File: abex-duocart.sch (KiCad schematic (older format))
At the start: 12 parts, among them P1 0877159106, P2 CONN_01X01, P3 CONN_01X01, P4 CONN_01X01, P5 CONN_01X01, SW2 SW_Push

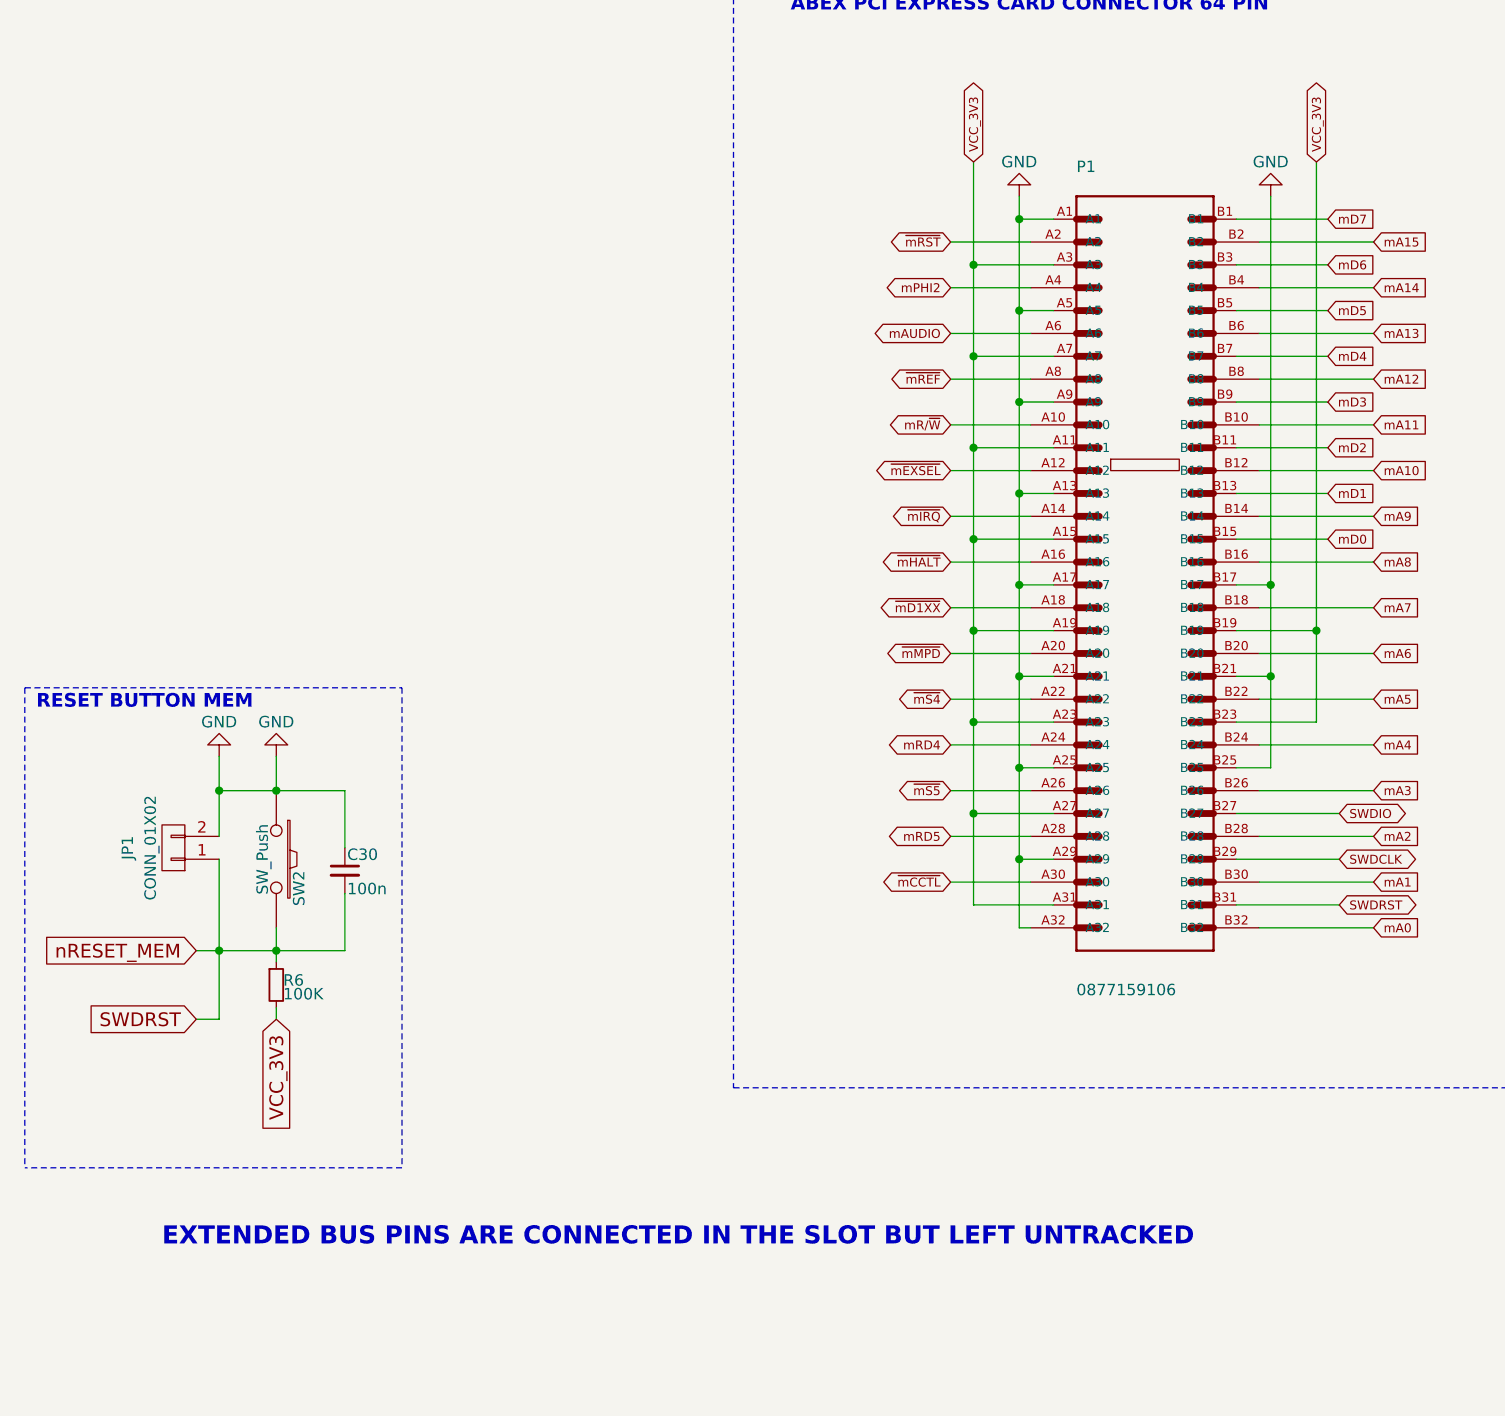
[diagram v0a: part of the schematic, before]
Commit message: Added the CardDetect. Added the A31 +5V pin
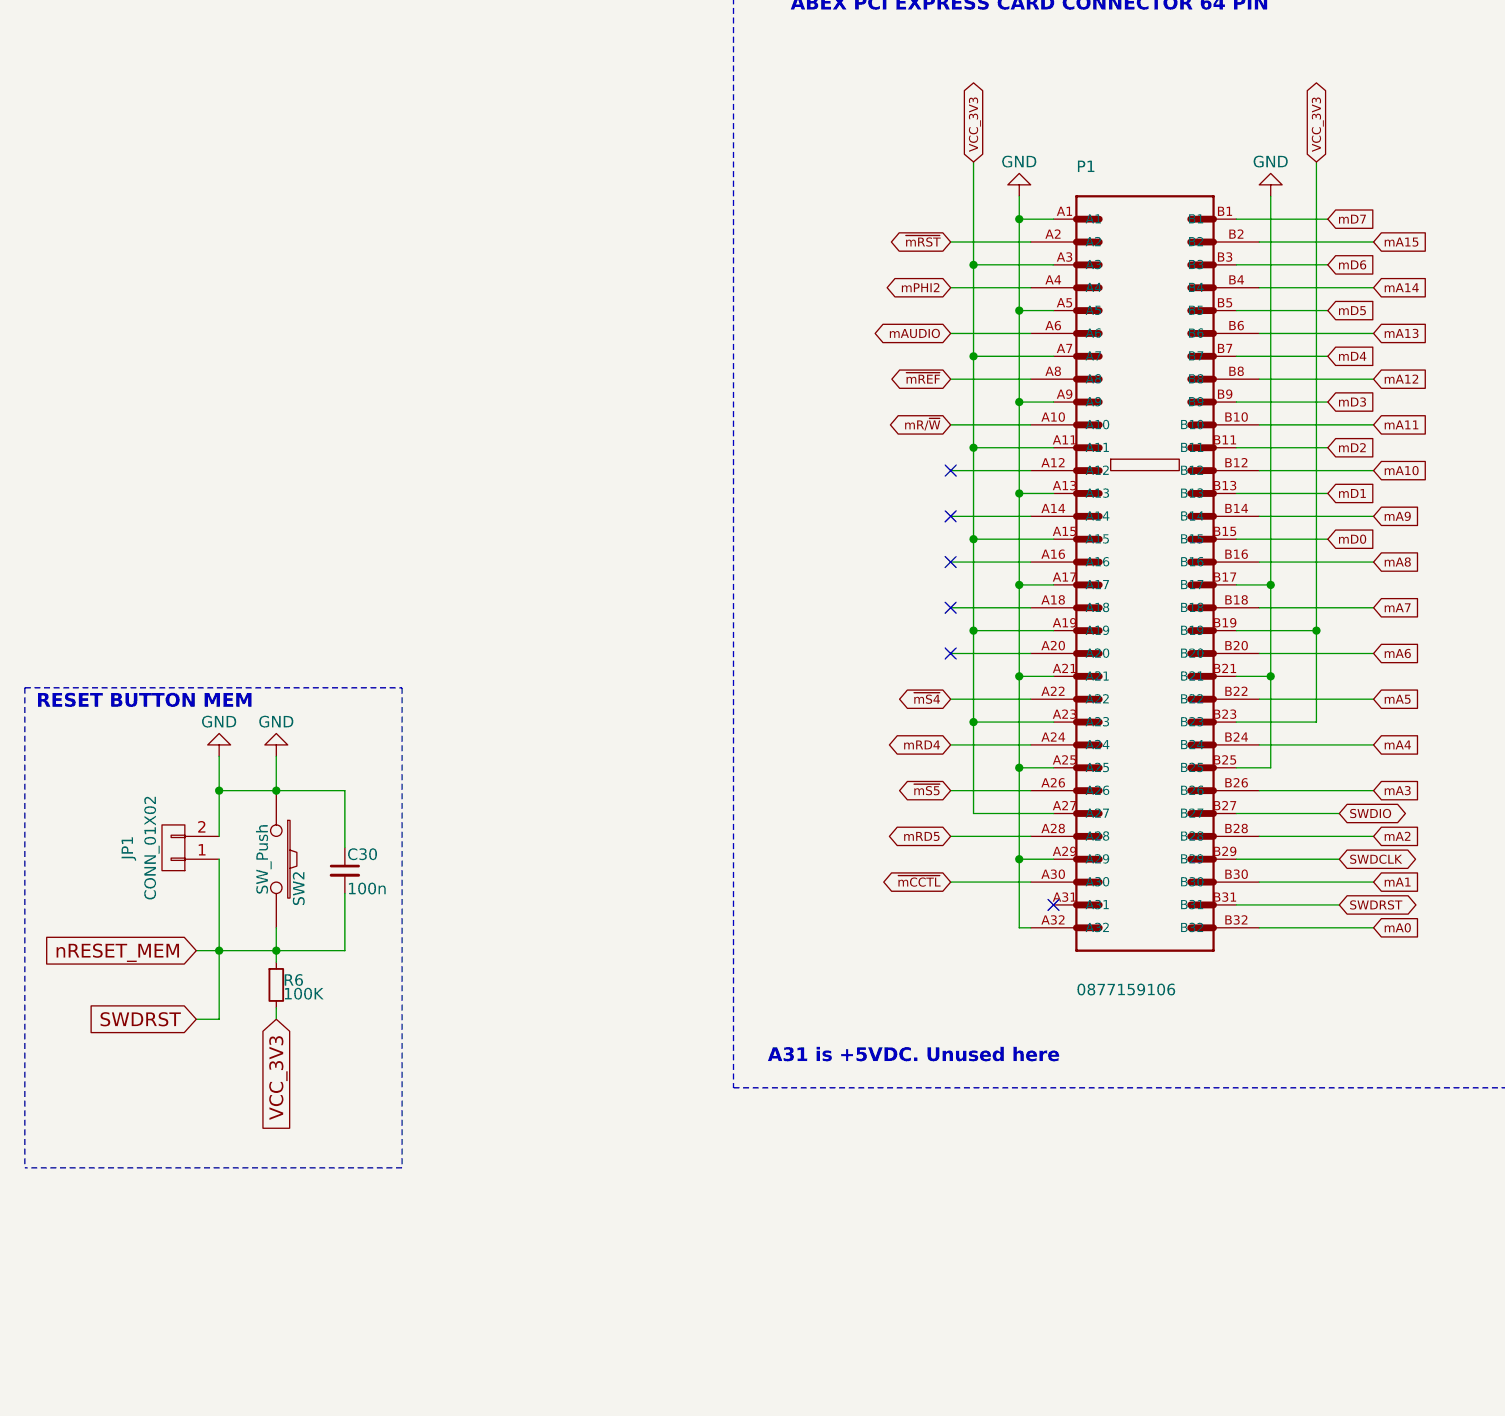
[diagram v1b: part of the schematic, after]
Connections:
- net VCC: no longer P1.A31
- net ~mD1XX: no longer names the net of P1.A18
- net ~mEXSEL: no longer names the net of P1.A12
- net ~mHALT: no longer names the net of P1.A16
- net ~mIRQ: no longer names the net of P1.A14
- net ~mMPD: no longer names the net of P1.A20
- no-connect marks 8 -> 14
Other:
- note added: "A31 is +5VDC. Unused here"
- note removed: "EXTENDED BUS PINS ARE CONNECTED IN THE SLOT BUT LEFT UNTRACKED"
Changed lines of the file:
@@
 LIBS:Graphic
 LIBS:GPU
-LIBS:ft232rl
 LIBS:FPGA_Xilinx_Virtex7
 LIBS:FPGA_Xilinx_Virtex6
@@
 Text GLabel 4750 2850 0    39   BiDi ~ 0
 mAUDIO
-Text GLabel 4750 3050 0    39   BiDi ~ 0
-~mREF
 Text GLabel 4850 2100 1    39   BiDi ~ 0
 VCC_3V3
@@
 Text GLabel 6450 4950 2    39   BiDi ~ 0
 SWDIO
-Text GLabel 4750 3450 0    39   BiDi ~ 0
-~mEXSEL
 Text GLabel 4750 3250 0    39   BiDi ~ 0
 mR/~W
-Text GLabel 4750 3650 0    39   BiDi ~ 0
-~mIRQ
-Text GLabel 4750 3850 0    39   BiDi ~ 0
-~mHALT
-Text GLabel 4750 4050 0    39   BiDi ~ 0
-~mD1XX
-Text GLabel 4750 4250 0    39   BiDi ~ 0
-~mMPD
 Text GLabel 4750 4450 0    39   BiDi ~ 0
 ~mS4
@@
 Text GLabel 6400 2350 2    39   Input ~ 0
 mD7
-Text Notes 1300 6850 0    79   ~ 16
-EXTENDED BUS PINS ARE CONNECTED IN THE SLOT BUT LEFT UNTRACKED
 Text GLabel 9700 4900 1    39   BiDi ~ 0
 SWDIO
@@
 Connection ~ 6150 4350
 Wire Wire Line
-	4850 2100 4850 5350
+	4850 2100 4850 4950
 Wire Wire Line
 	4850 2550 5200 2550
@@
 	4850 4950 5200 4950
 Connection ~ 4850 4550
-Wire Wire Line
-	4850 5350 5200 5350
-Connection ~ 4850 4950
 Wire Wire Line
 	6000 4550 6350 4550
@@
 Wire Wire Line
 	1800 5450 1800 5600
+NoConn ~ 5200 5350
+Text Notes 3950 6050 0    60   ~ 12
+A31 is +5VDC. Unused here
+Text GLabel 4750 3050 0    39   BiDi ~ 0
+~mREF
+NoConn ~ 4750 3450
+NoConn ~ 4750 3650
+NoConn ~ 4750 3850
+NoConn ~ 4750 4050
+NoConn ~ 4750 4250
 $EndSCHEMATC
